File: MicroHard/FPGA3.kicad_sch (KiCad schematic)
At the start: 26 parts, among them J1 FPGA_DEBUG, Q1 2N7002_SOT-23-3, Q2 2N7002_SOT-23-3, Q3 2N7002_SOT-23-3, Q4 2N7002_SOT-23-3, Q5 2N7002_SOT-23-3, U4 XC7A100T-FTG256

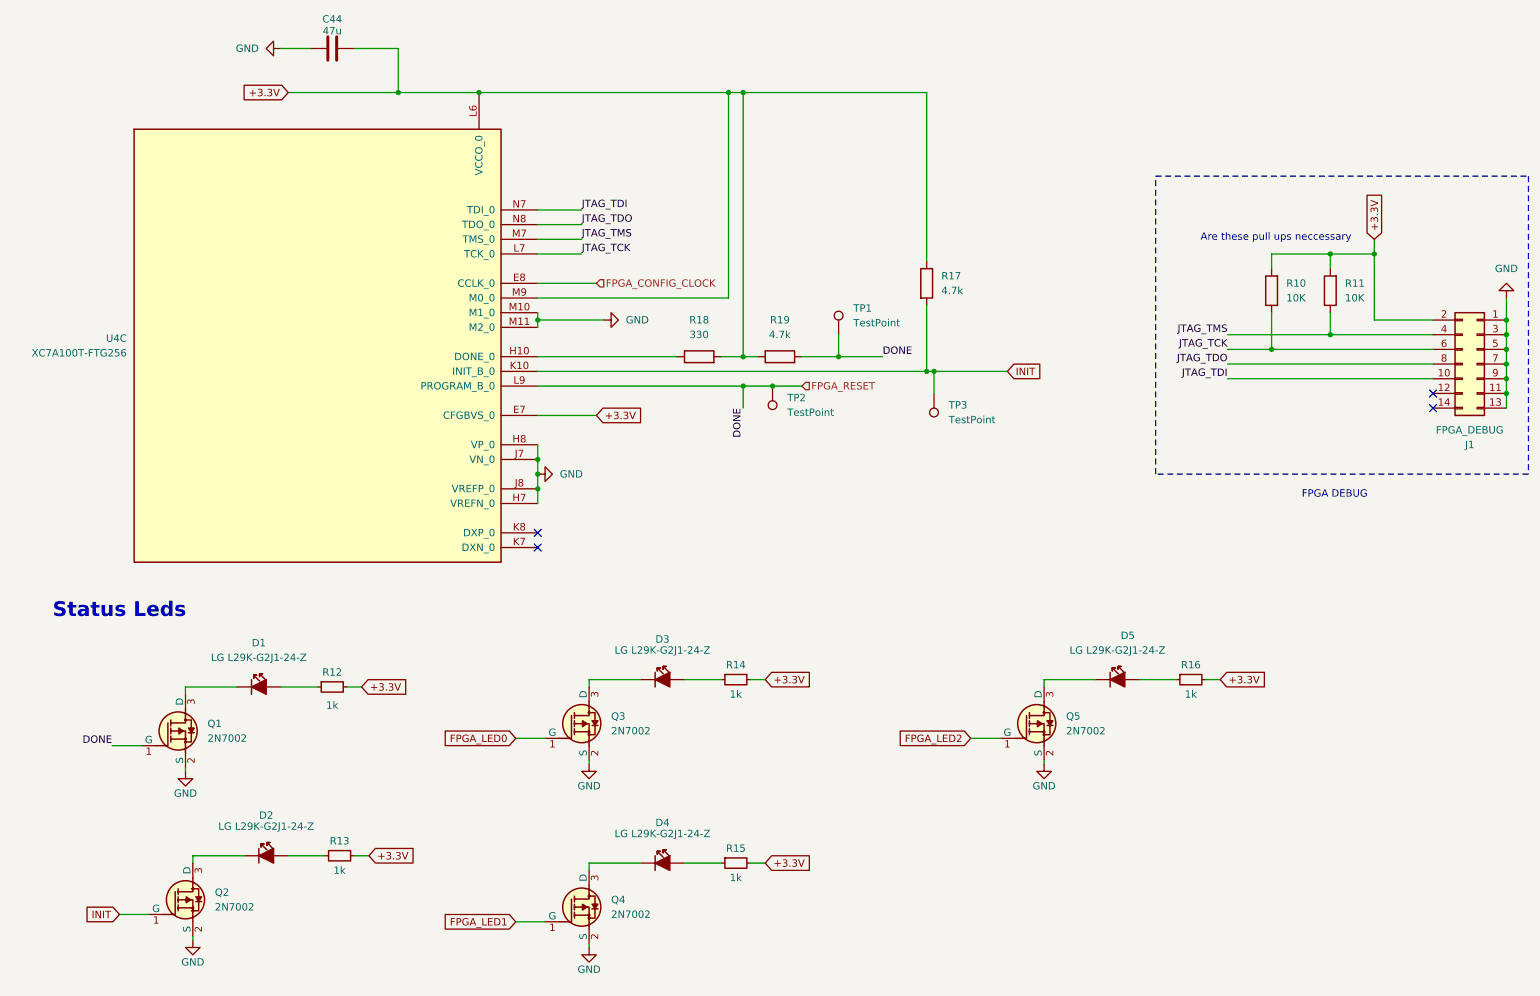
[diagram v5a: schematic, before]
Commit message: feat: added VGA signal out from FPGA
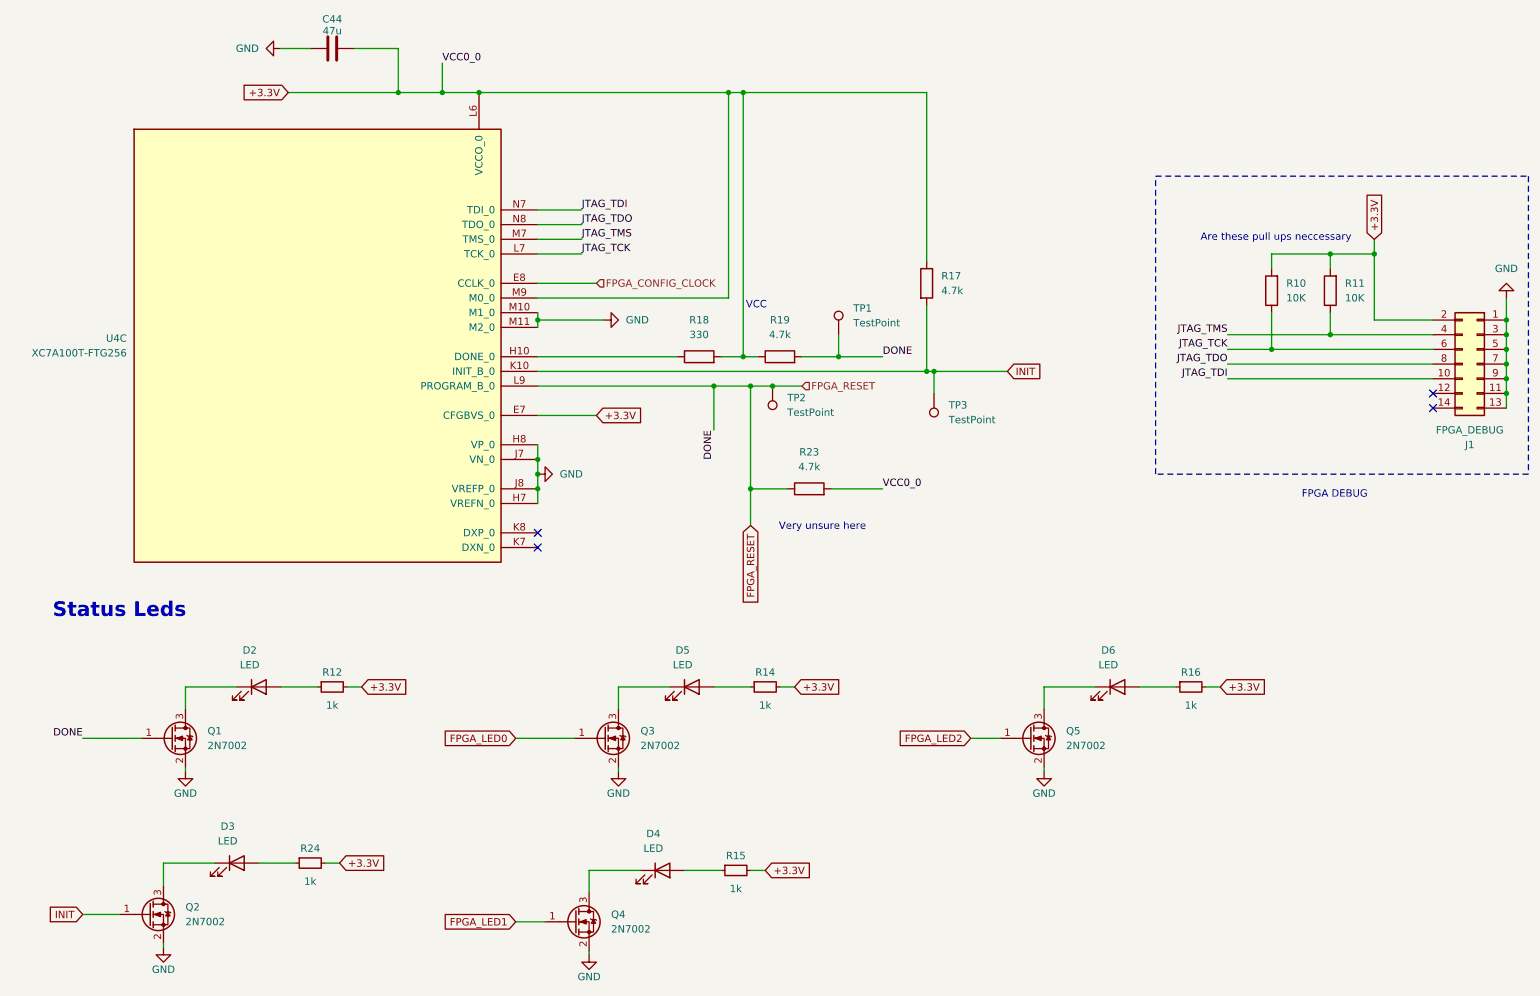
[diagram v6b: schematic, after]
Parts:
- removed D1, D2, D3, D4, D5: LED_G_0603_LG_L29K-G2J1-24-Z, antmicro-footprints:LED_0603_1608Metric_G, symbol antmicroLEDIndicationDiscrete:LED_G_0603_LG_L29K-G2J1-24-Z
- removed Q1, Q2, Q3, Q4, Q5: 2N7002_SOT-23-3, antmicro-footprints:SOT-23-3, symbol antmicroTransistorsFETsMOSFETsSingle:2N7002_SOT-23-3
- removed R13: R_1k_0402, antmicro-footprints:R_0402_1005Metric, symbol antmicroResistors0402:R_1k_0402
- added D2, D3, D4, D5, D6: LED, symbol Device:LED
- added Q1, Q2, Q3, Q4, Q5: 2N7002, Package_TO_SOT_SMD:SOT-23, symbol Transistor_FET:2N7002
- added R23: 4.7k, symbol Device:R
- added R24: R_1k_0402, antmicro-footprints:R_0402_1005Metric, symbol antmicroResistors0402:R_1k_0402
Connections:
- net +3.3V: now also R23.2, R24.2
- net FPGA_LED0: now also Q3.1 (G)
- net FPGA_LED1: now also Q4.1 (G)
- net FPGA_LED2: now also Q5.1 (G)
- net FPGA_RESET: now also Q1.1 (G), R23.1
- net GND: now also Q1.2 (S), Q2.2 (S), Q3.2 (S), Q4.2 (S), Q5.2 (S)
- net INIT: now also Q2.1 (G)
- net at R12.1: now also D2.2 (A)
- net at R16.1: now also D6.2 (A)
- net at R14.1: now also D5.2 (A)
- net at R15.1: now also D4.2 (A)
- new net: D5.1 (K), Q3.3 (D)
- new net: D3.1 (K), Q2.3 (D)
- new net: D3.2 (A), R24.1
- new net: D4.1 (K), Q4.3 (D)
- new net: D2.1 (K), Q1.3 (D)
- new net: D6.1 (K), Q5.3 (D)
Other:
- note added: "VCC"
- note added: "Very unsure here"

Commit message: feat: VGA out lines from FPGA drawn
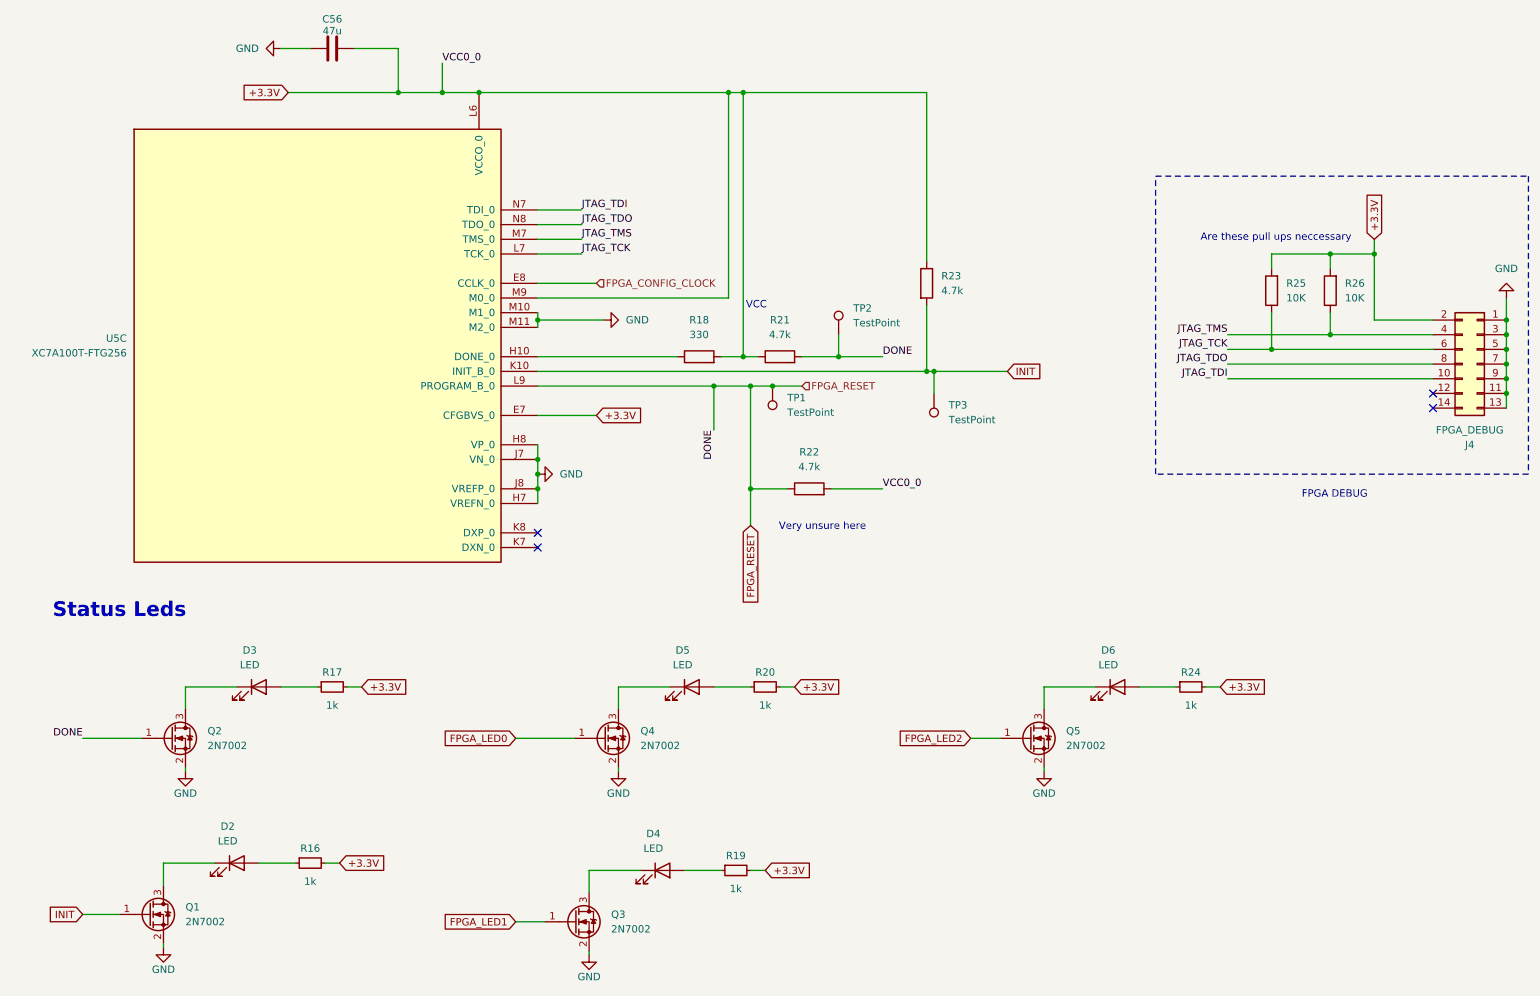
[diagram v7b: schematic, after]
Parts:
- renumbered C44 to C56, D3 to D2, D2 to D3, J1 to J4, Q2 to Q1, Q1 to Q2, Q4 to Q3, Q3 to Q4, R24 to R16, R12 to R17, R15 to R19, R14 to R20, R19 to R21, R23 to R22, R17 to R23, R16 to R24, R10 to R25, R11 to R26, TP2 to TP1, TP1 to TP2, U4 to U5

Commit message: feat: finished schematic, TODO: go through checklist
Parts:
- removed D6: LED, symbol Device:LED
- removed Q1, Q2, Q3, Q4, Q5: 2N7002, Package_TO_SOT_SMD:SOT-23, symbol Transistor_FET:2N7002
- removed R16, R17, R19, R20, R24: R_1k_0402, antmicro-footprints:R_0402_1005Metric, symbol antmicroResistors0402:R_1k_0402
- removed R18: 330, symbol Device:R
- removed R21: 4.7k, symbol Device:R
- added R22: 100, symbol Device:R
- added R23, R25, R26: 330, symbol Device:R
- added R61: 200, symbol Device:R
- U5: footprint (none) -> MicroHard:BGA256C100P16X16_1700X1700X155
- renumbered R22 to R62, R23 to R63, R25 to R64, R26 to R65
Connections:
- net +3.3V: now also R61.1
- net FPGA_LED0: now also R23.2
- net FPGA_LED1: now also R25.2
- net FPGA_LED2: now also R26.2
- net FPGA_RESET: no longer TP2.1
- net GND: now also D2.1 (K), D3.1 (K), D4.1 (K), D5.1 (K)
- net at D3.2 (A): now also R23.1
- net at D5.2 (A): now also R26.1
- net at D2.2 (A): now also R22.2
- net DONE: now reaches U5.H10 (DONE_0)
- net DONE: now also TP2.1, R22.1, R61.2
- net at D4.2 (A): now also R25.1
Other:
- note removed: "VCC"
- moved on the sheet: TP3
